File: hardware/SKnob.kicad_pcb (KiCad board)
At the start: 2 copper layers, 61 x 17 mm, 2 parts, among them U1 STM32WLE5JCI6

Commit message: rf network
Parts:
- added C1: C, Capacitor_SMD:C_0402_1005Metric, F.Cu at (126.0, 97.0)
- added C10: C, Capacitor_SMD:C_0402_1005Metric, F.Cu at (116.6, 104.5)
- added C11: C, Capacitor_SMD:C_0402_1005Metric, F.Cu at (123.1, 95.0)
- added C12: C, Capacitor_SMD:C_0402_1005Metric, F.Cu at (128.9, 95.0)
- added C13: C, Capacitor_SMD:C_0402_1005Metric, F.Cu at (119.5, 103.0)
- added C2: C, Capacitor_SMD:C_0402_1005Metric, F.Cu at (108.0, 97.0)
- added C3: C, Capacitor_SMD:C_0402_1005Metric, F.Cu at (120.2, 97.0)
- added C4: C, Capacitor_SMD:C_0402_1005Metric, F.Cu at (106.5, 94.5)
- added C5: C, Capacitor_SMD:C_0402_1005Metric, F.Cu at (106.0, 96.0)
- added C6: C, Capacitor_SMD:C_0402_1005Metric, F.Cu at (123.1, 97.0)
- added C7: C, Capacitor_SMD:C_0402_1005Metric, F.Cu at (126.0, 95.0)
- added C8: C, Capacitor_SMD:C_0402_1005Metric, F.Cu at (120.2, 101.0)
- added C9: C, Capacitor_SMD:C_0402_1005Metric, F.Cu at (123.1, 99.0)
- added L1: L, Inductor_SMD:L_0402_1005Metric, F.Cu at (108.0, 95.0)
- added L2: L, Inductor_SMD:L_0402_1005Metric, F.Cu at (111.5, 99.0)
- added L3: L, Inductor_SMD:L_0402_1005Metric, F.Cu at (119.5, 105.0)
- added L4: L, Inductor_SMD:L_0402_1005Metric, F.Cu at (128.9, 97.0)
- added L5: L, Inductor_SMD:L_0402_1005Metric, F.Cu at (122.5, 103.0)
- added L6: L, Inductor_SMD:L_0402_1005Metric, F.Cu at (126.0, 101.0)
- added U2: BGS12SN6, Package_BGA:Texas_DSBGA-6_0.9x1.4mm_Layout2x3_P0.5mm, F.Cu at (113.2, 103.8)
- moved U1 11.7 mm to (113.0, 95.0), turned to 270 degrees
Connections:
- U1 pad H7: Net-(U1-PadH7) -> /RFI_N
- U1 pad J6: Net-(U1-PadJ6) -> /RFI_P
- U1 pad J8: Net-(U1-PadJ8) -> /RFO_LP

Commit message: stm32wb chip selection
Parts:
- removed C11, C12, C13: C, Capacitor_SMD:C_0402_1005Metric
- removed L4, L5, L6: L, Inductor_SMD:L_0402_1005Metric
- removed U2: BGS12SN6, Package_BGA:Texas_DSBGA-6_0.9x1.4mm_Layout2x3_P0.5mm
- added ANT1: W3008, SKnob:W3008, F.Cu at (104.8, 78.2)
- added J1: USB_B_Micro, Connector_USB:USB_Micro-B_Molex-105133-0001, F.Cu at (124.9, 84.5)
- C1, C2, C3, C4, C7, C8: value C -> 100nF
- C5, C6: value C -> 100pF
- L1, L2: footprint Inductor_SMD:L_0402_1005Metric -> Inductor_SMD:L_0603_1608Metric
- U1: value STM32WLE5JCI6 -> STM32WB55Cx; footprint SKnob:STM32WLE5JCI6 -> SKnob:STM32WB55Cx
- moved L3 24.6 mm to (108.4, 83.0), turned to 180 degrees
- moved C10 24.1 mm to (107.0, 82.4), turned to 90 degrees
- moved L1 21.5 mm to (116.8, 75.4), turned to 0 degrees
- moved C9 21.3 mm to (109.8, 82.4), turned to 90 degrees
- moved C1 21.2 mm to (119.8, 76.8)
- moved C4 20.3 mm to (116.2, 76.8)
- moved C7 19.0 mm to (110.0, 84.8), turned to 270 degrees
- moved C3 17.5 mm to (121.2, 79.5), turned to 270 degrees
- moved C2 16.0 mm to (111.0, 81.2), turned to 90 degrees
- moved C8 14.3 mm to (118.5, 86.8), turned to 180 degrees
- moved L2 14.0 mm to (108.6, 85.3), turned to 270 degrees
- moved U1 13.6 mm to (116.2, 81.8)
- moved C6 13.6 mm to (121.2, 83.5), turned to 270 degrees
- moved C5 12.3 mm to (111.0, 84.8)
- turned BT1 to 0 degrees
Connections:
- C1 pad 1: Net-(C1-Pad1) -> +BATT
- C10 pad 1: Net-(C10-Pad1) -> Net-(ANT1-PadFEED)
- C2 pad 1: /RFI_N -> +BATT
- C2 pad 2: GND -> Net-(C2-Pad2)
- C3 pad 1: Net-(C1-Pad1) -> +BATT
- C3 pad 2: GND -> Net-(C3-Pad2)
- C4 pad 2: /RFI_P -> GND
- C5 pad 1: Net-(C4-Pad1) -> Net-(C5-Pad1)
- C6 pad 1: Net-(C6-Pad1) -> +5V
- C7 pad 1: Net-(C7-Pad1) -> Net-(C5-Pad1)
- C7 pad 2: Net-(C6-Pad1) -> GND
- C8 pad 1: Net-(C7-Pad1) -> +BATT
- C8 pad 2: GND -> Net-(C8-Pad2)
- C9 pad 2: Net-(C7-Pad1) -> GND
- L1 pad 1: /RFI_P -> Net-(C4-Pad1)
- L1 pad 2: /RFI_N -> +BATT
- L2 pad 1: /RFO_LP -> Net-(C5-Pad1)
- L2 pad 2: Net-(C6-Pad1) -> +BATT
- L3 pad 1: Net-(C1-Pad1) -> Net-(C9-Pad1)
- L3 pad 2: Net-(C6-Pad1) -> Net-(ANT1-PadFEED)
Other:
- net class Default: via_dia 0.3 -> 0.5; via_drill 0.1 -> 0.3
- rule pad_to_mask_clearance: 0.05 -> 0

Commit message: preliminary routing
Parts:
- added C11: 100nF, Capacitor_SMD:C_0402_1005Metric, F.Cu at (120.0, 81.7)
- added C12: 100nF, Capacitor_SMD:C_0402_1005Metric, F.Cu at (120.3, 77.1)
- added C13: 4.7uF, Capacitor_SMD:C_0805_2012Metric, F.Cu at (113.6, 87.1)
- added C14: 100nF, Capacitor_SMD:C_0402_1005Metric, F.Cu at (118.0, 86.2)
- added C15: 4.7uF, Capacitor_SMD:C_0805_2012Metric, F.Cu at (119.5, 87.0)
- added C16: C, Capacitor_SMD:C_0402_1005Metric, F.Cu at (111.7, 85.9)
- added C17: C, Capacitor_SMD:C_0402_1005Metric, F.Cu at (117.7, 75.7)
- added C18: C, Capacitor_SMD:C_0402_1005Metric, F.Cu at (109.8, 85.9)
- added C19: C, Capacitor_SMD:C_0402_1005Metric, F.Cu at (115.8, 75.7)
- added C20: 4.7uF, Capacitor_SMD:C_0805_2012Metric, F.Cu at (123.6, 78.3)
- added C21: 100nF, Capacitor_SMD:C_0402_1005Metric, F.Cu at (122.0, 78.2)
- added C22: 100nF, Capacitor_SMD:C_0402_1005Metric, F.Cu at (130.8, 75.6)
- added C23: 4.7uF, Capacitor_SMD:C_0805_2012Metric, F.Cu at (132.4, 75.9)
- added C24: 100nF, Capacitor_SMD:C_0402_1005Metric, F.Cu at (129.8, 75.6)
- added C25: 4.7uF, Capacitor_SMD:C_0805_2012Metric, F.Cu at (130.6, 84.9)
- added C26: 4.7uF, Capacitor_SMD:C_0805_2012Metric, F.Cu at (132.6, 84.9)
- added D1: D, Diode_SMD:D_0603_1608Metric, F.Cu at (120.4, 73.9)
- added D2: TPD4S012DRYR, SKnob:TPD4S012DRYR, F.Cu at (121.2, 83.6)
- added J2: Conn_01x02, Connector_PinHeader_1.00mm:PinHeader_1x02_P1.00mm_Vertical, F.Cu at (125.8, 77.6)
- added J3: Conn_01x02, Connector_PinHeader_1.00mm:PinHeader_1x02_P1.00mm_Vertical, F.Cu at (130.2, 77.6)
- added L4: 600R @ 100MHz, Inductor_SMD:L_0402_1005Metric, F.Cu at (115.6, 85.7)
- added R1: R, Resistor_SMD:R_0402_1005Metric, F.Cu at (121.6, 81.5)
- added R2: R, Resistor_SMD:R_0402_1005Metric, F.Cu at (113.8, 73.0)
- added R3: 10K, Resistor_SMD:R_0402_1005Metric, F.Cu at (111.4, 73.0)
- added R4: 10k, Resistor_SMD:R_0402_1005Metric, F.Cu at (109.1, 73.0)
- added SW1: SW_Push, Button_Switch_SMD:SW_SPST_B3U-3000P, F.Cu at (123.8, 73.9)
- added Y1: 32MHz, Crystal:Crystal_SMD_2016-4Pin_2.0x1.6mm, F.Cu at (110.6, 87.7)
- added Y2: 32MHz, Crystal:Crystal_SMD_2016-4Pin_2.0x1.6mm, F.Cu at (116.8, 73.7)
- BT1: value Battery_Cell -> BR1225
- C1: value 100nF -> C
- C10: value C -> 0.3pF
- C6: value 100pF -> 4.7uF; footprint Capacitor_SMD:C_0402_1005Metric -> Capacitor_SMD:C_0805_2012Metric
- C9: value C -> 0.8pF
- L1, L2: value L -> 600R @ 100MHz
- L3: value L -> 2.7nF
- moved BT1 12.0 mm to (141.0, 80.5)
- moved L1 4.14 mm to (112.8, 74.5), turned to 180 degrees
- moved C1 4.13 mm to (121.6, 80.5), turned to 180 degrees
- moved C10 3.52 mm to (106.1, 79.0), turned to 45 degrees
- moved C6 3.52 mm to (121.6, 87.0)
- moved L3 3.13 mm to (106.7, 80.3), turned to 135 degrees
- moved C4 3.08 mm to (113.4, 75.7), turned to 180 degrees
- moved ANT1 3.05 mm to (104.6, 75.2)
- moved C9 2.23 mm to (108.1, 81.0), turned to 45 degrees
- moved U1 1.84 mm to (114.8, 80.7)
- moved C2 1.82 mm to (109.8, 79.9)
- moved C3 1.75 mm to (120.3, 78.1), turned to 0 degrees
- moved C8 1.63 mm to (117.0, 86.2), turned to 270 degrees
- moved C5 1.32 mm to (109.8, 84.3)
- moved C7 1.32 mm to (108.8, 84.3)
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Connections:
- net Net-(ANT1-PadFEED) renamed /RF1_ANT
- net Net-(C9-Pad1) renamed /RF1
- C1 pad 1: +BATT -> Net-(C1-Pad1)
- C2 pad 2: Net-(C2-Pad2) -> GND
- C3 pad 2: Net-(C3-Pad2) -> GND
- C8 pad 2: Net-(C8-Pad2) -> GND
- J1 pad 1: Net-(J1-Pad1) -> +5V
- J1 pad 2: Net-(J1-Pad2) -> /USB_N
- J1 pad 3: Net-(J1-Pad3) -> /USB_P
- J1 pad 4: Net-(J1-Pad4) -> /ID
- J1 pad 5: Net-(J1-Pad5) -> GND
- J1 pad 6: Net-(J1-Pad6) -> Net-(C1-Pad1)
- U1 pad 2: Net-(U1-Pad2) -> /OSC32_IN
- U1 pad 22: Net-(U1-Pad22) -> GND
- U1 pad 24: Net-(U1-Pad24) -> /OSC_OUT
- U1 pad 25: Net-(U1-Pad25) -> /OSC_IN
- U1 pad 3: Net-(U1-Pad3) -> /OSC32_OUT
- U1 pad 32: Net-(U1-Pad32) -> GND
- U1 pad 34: Net-(U1-Pad34) -> +BATT
- U1 pad 37: Net-(U1-Pad37) -> /USB_N
- U1 pad 38: Net-(U1-Pad38) -> /USB_P
- U1 pad 4: Net-(U1-Pad4) -> /BOOT
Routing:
- net GND: track 0.00 -> 28.4 mm, vias 0 -> 37
- net +BATT: track 0.00 -> 21.1 mm, vias 0 -> 31
- net Net-(D1-Pad2): track 0.00 -> 10.6 mm, vias 0 -> 2
- net /BOOT: track 0.00 -> 9.06 mm, vias 0 -> 2
- net +5V: track 0.00 -> 7.72 mm, vias 0 -> 2
- net /OSC_OUT: track 0.00 -> 5.78 mm
- net Net-(C13-Pad1): track 0.00 -> 4.89 mm
- net /OSC32_IN: track 0.00 -> 4.84 mm
- net /RF1: track 0.00 -> 4.82 mm
- net Net-(C5-Pad1): track 0.00 -> 4.22 mm
- net /RF1_ANT: track 0.00 -> 3.75 mm
- net /OSC_IN: track 0.00 -> 3.47 mm
- net /OSC32_OUT: track 0.00 -> 3.26 mm
- net Net-(C4-Pad1): track 0.00 -> 3.02 mm
- net Net-(D1-Pad1): track 0.00 -> 2.03 mm
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- added copper zone on F.Cu, net +BATT
- added copper zone on In2.Cu, net +BATT
- added copper zone on B.Cu, net GND
- added copper zone on F.Cu, net GND
- added copper zone on In1.Cu, net GND
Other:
- board size 61 x 17 mm -> 50 x 17 mm
- copper layers 2 -> 4
- net class Default: via_dia 0.5 -> 0.45; via_drill 0.3 -> 0.2
- net class microstrip added: clearance 0.3, trace_width 0.29337, via_dia 0.45, via_drill 0.2
- net class pwr added: clearance 0.15, trace_width 0.3, via_dia 0.6, via_drill 0.3
- rule trace_min: 0.15 -> 0.127

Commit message: added accel
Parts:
- added C27: 100nF, Capacitor_SMD:C_0402_1005Metric, F.Cu at (109.4, 77.4)
- added U2: LIS2DE12TR, SKnob:LIS2DE12TR, F.Cu at (109.4, 75.6)
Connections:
- U1 pad 5: Net-(U1-Pad5) -> /I2C1_SCL
- U1 pad 6: Net-(U1-Pad6) -> /I2C1_SDA
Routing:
- net /I2C1_SDA: track 0.00 -> 9.03 mm, vias 0 -> 2
- net /I2C1_SCL: track 0.00 -> 8.65 mm, vias 0 -> 2
- net GND: track 28.4 -> 32.0 mm, vias 37 -> 38
- net +BATT: track 21.1 -> 24.1 mm, vias 31 -> 32

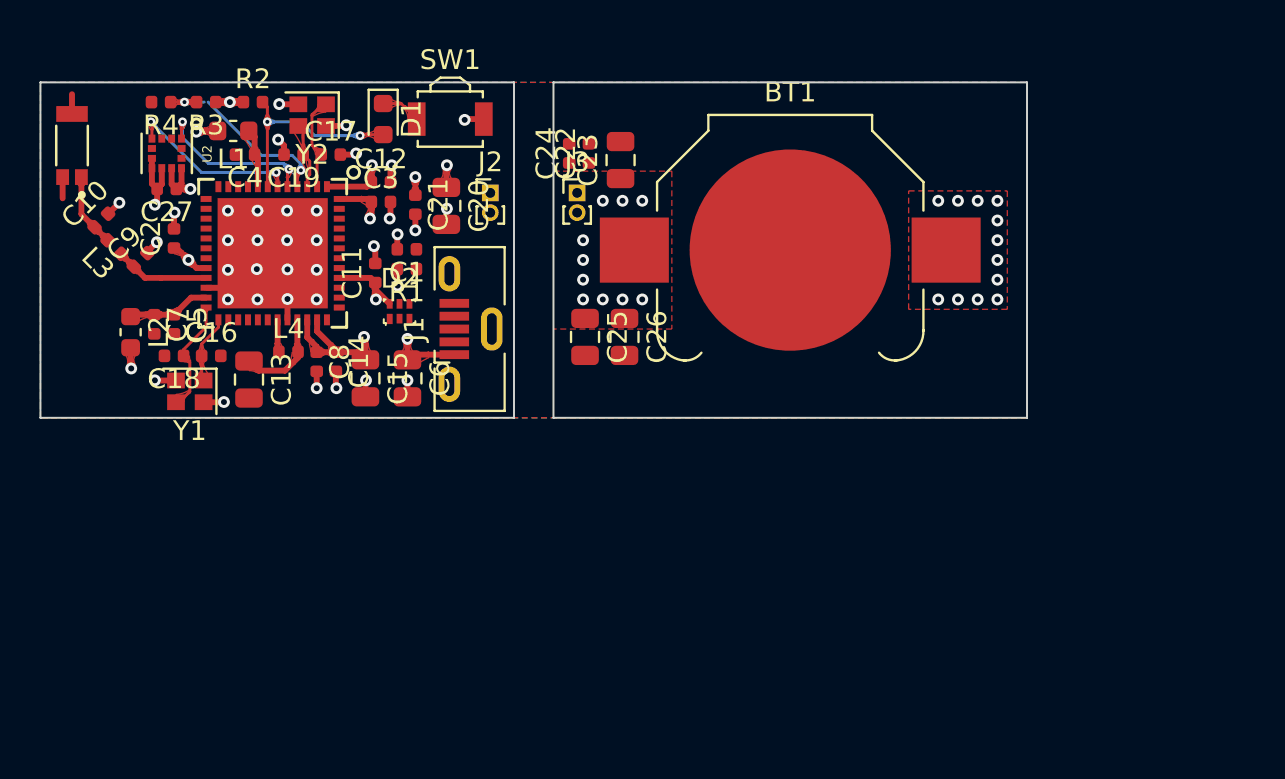
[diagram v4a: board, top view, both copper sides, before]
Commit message: update hardware to include test points in the back and commit auto generated firmware project files
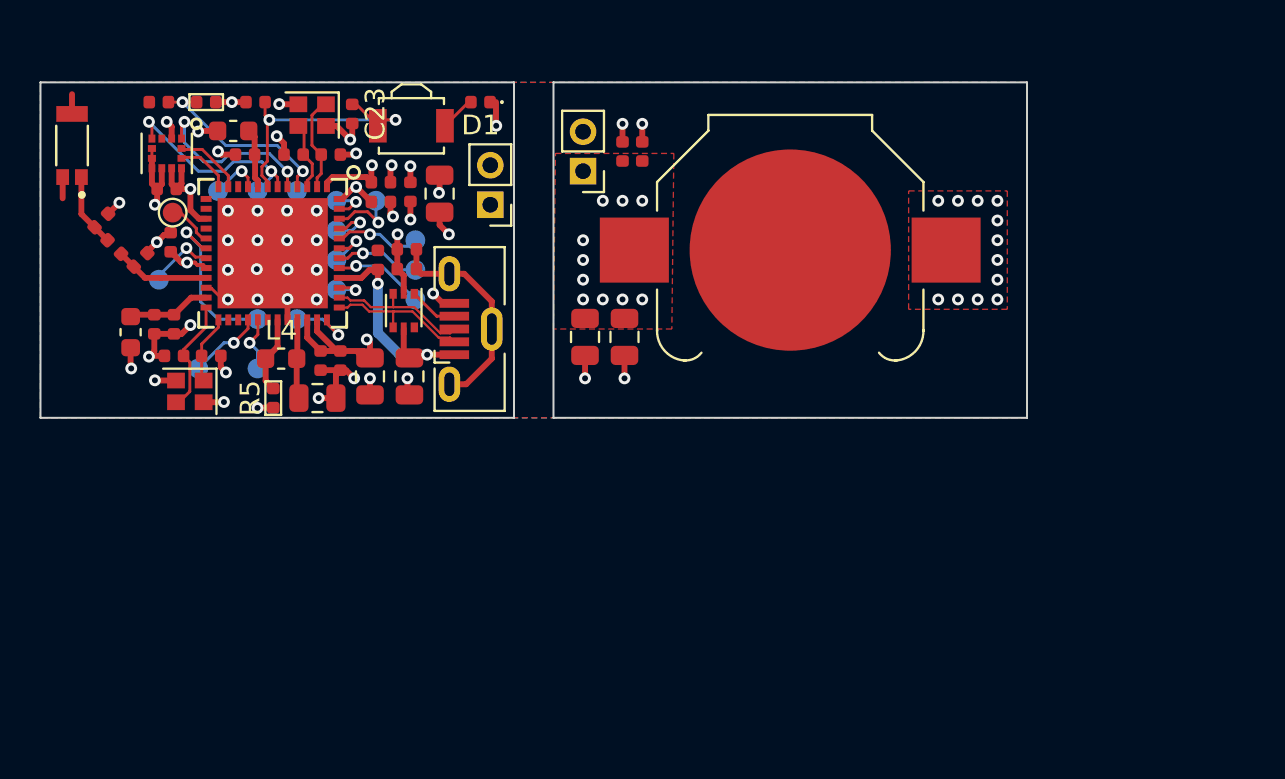
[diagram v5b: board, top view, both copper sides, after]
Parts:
- removed D2: TPD4S012DRYR, SKnob:TPD4S012DRYR
- added R5: 0, SKnob:R_0402_1005Metric_DNP, F.Cu at (114.8, 88.0)
- added T1: LA_LOGO, SKnob:LA_LOGO, F.Cu at (105.5, 87.0)
- added T2: LA_LOGO, SKnob:LA_LOGO, F.Cu at (150.5, 87.0)
- added TP1: TestPoint, SKnob:TestPoint_Pad_D1.0mm, F.Cu at (109.7, 78.6)
- added TP10: TestPoint, SKnob:TestPoint_Pad_D1.0mm, B.Cu at (122.0, 80.0)
- added TP11: TestPoint, SKnob:TestPoint_Pad_D1.0mm, B.Cu at (118.0, 79.5)
- added TP12: TestPoint, SKnob:TestPoint_Pad_D1.0mm, B.Cu at (120.0, 78.0)
- added TP13: TestPoint, SKnob:TestPoint_Pad_D1.0mm, B.Cu at (118.0, 78.0)
- added TP14: TestPoint, SKnob:TestPoint_Pad_D1.0mm, B.Cu at (118.0, 82.5)
- added TP15: TestPoint, SKnob:TestPoint_Pad_D1.0mm, B.Cu at (122.0, 83.0)
- added TP16: TestPoint, SKnob:TestPoint_Pad_D1.0mm, B.Cu at (122.0, 81.5)
- added TP17: TestPoint, SKnob:TestPoint_Pad_D1.0mm, B.Cu at (112.0, 77.5)
- added TP2: TestPoint, SKnob:TestPoint_Pad_D1.0mm, B.Cu at (116.0, 77.5)
- added TP3: TestPoint, SKnob:TestPoint_Pad_D1.0mm, B.Cu at (114.0, 77.5)
- added TP4: TestPoint, SKnob:TestPoint_Pad_D1.0mm, B.Cu at (114.0, 84.0)
- added TP5: TestPoint, SKnob:TestPoint_Pad_D1.0mm, B.Cu at (116.0, 84.0)
- added TP6: TestPoint, SKnob:TestPoint_Pad_D1.0mm, B.Cu at (111.0, 86.5)
- added TP7: TestPoint, SKnob:TestPoint_Pad_D1.0mm, B.Cu at (114.0, 86.5)
- added TP8: TestPoint, SKnob:TestPoint_Pad_D1.0mm, B.Cu at (109.0, 82.0)
- added TP9: TestPoint, SKnob:TestPoint_Pad_D1.0mm, B.Cu at (118.0, 81.0)
- added U3: USBLC6-2P6, Package_TO_SOT_SMD:SOT-666, F.Cu at (121.4, 83.6)
- C16, C17, C18, C19: value C -> 4.3pF
- C23: value 4.7uF -> 100nF; footprint Capacitor_SMD:C_0805_2012Metric -> Capacitor_SMD:C_0402_1005Metric
- D1: value D -> 1N4148; footprint Diode_SMD:D_0603_1608Metric -> Diode_SMD:D_0402_1005Metric
- J2, J3: footprint Connector_PinHeader_1.00mm:PinHeader_1x02_P1.00mm_Vertical -> Connector_PinHeader_2.00mm:PinHeader_1x02_P2.00mm_Vertical
- L4: value 600R @ 100MHz -> 10uH; footprint Inductor_SMD:L_0402_1005Metric -> Inductor_SMD:L_0603_1608Metric
- R2: value R -> 10k
- R3: footprint Resistor_SMD:R_0402_1005Metric -> SKnob:R_0402_1005Metric_DNP
- Y2: value 32MHz -> 32.768kHz
- moved C23 13.8 mm to (118.8, 73.6), turned to 270 degrees
- moved D1 5.00 mm to (125.3, 73.0), turned to 180 degrees
- moved C13 3.59 mm to (117.0, 88.0), turned to 0 degrees
- moved C22 2.70 mm to (133.5, 75.5)
- moved C24 2.70 mm to (132.5, 75.5)
- moved SW1 2.00 mm to (121.8, 74.2)
- moved J3 1.14 mm to (130.5, 76.5), turned to 180 degrees
- moved C20 0.71 mm to (123.2, 77.6), turned to 90 degrees
- moved C21 0.70 mm to (121.8, 77.5), turned to 90 degrees
- moved C11 0.67 mm to (120.1, 81.0)
- moved J2 0.60 mm to (125.8, 78.2), turned to 180 degrees
- moved L4 0.50 mm to (115.2, 86.0)
- moved C2 0.25 mm to (109.6, 80.1)
- moved C15 0.25 mm to (119.7, 86.9)
- moved C14 0.24 mm to (118.2, 86.1)
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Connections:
- net Net-(C4-Pad1) renamed /VDDA
- net Net-(C5-Pad1) renamed /VDDRF
- C23 pad 1: +BATT -> /RST_N
- D1 pad 1: Net-(D1-Pad1) -> GND
- R2 pad 2: Net-(D1-Pad2) -> /RST_N
- SW1 pad 1: Net-(D1-Pad1) -> /RST_N
- SW1 pad 2: GND -> Net-(D1-Pad2)
- U1 pad 11: Net-(U1-Pad11) -> /ACC_INT1
- U1 pad 12: Net-(U1-Pad12) -> /ACC_INT2
- U1 pad 15: Net-(U1-Pad15) -> +BATT
- U1 pad 17: Net-(U1-Pad17) -> /RCC_MCO
- U1 pad 18: Net-(U1-Pad18) -> /USART1_TX
- U1 pad 19: Net-(U1-Pad19) -> /PB2
- U1 pad 28: Net-(U1-Pad28) -> /PB0
- U1 pad 29: Net-(U1-Pad29) -> /PB1
- U1 pad 36: Net-(U1-Pad36) -> /USART1_RX
- U1 pad 39: Net-(U1-Pad39) -> /JTMS-SWDIO
- U1 pad 41: Net-(U1-Pad41) -> /JTCK-SWCLK
- U1 pad 42: Net-(U1-Pad42) -> /JTDI
- U1 pad 43: Net-(U1-Pad43) -> /PB3_JTDO-SWO
- U1 pad 44: Net-(U1-Pad44) -> /PB4_JTRST
- U1 pad 45: Net-(U1-Pad45) -> /PB5
- U1 pad 46: Net-(U1-Pad46) -> /PB6
- U1 pad 47: Net-(U1-Pad47) -> /PB7
- U1 pad 7: Net-(D1-Pad2) -> /RST_N
- U1 pad 9: Net-(U1-Pad9) -> /WKUP1
- U2 pad 11: Net-(U2-Pad11) -> /ACC_INT2
- U2 pad 12: Net-(U2-Pad12) -> /ACC_INT1
- U2 pad 2: Net-(U2-Pad2) -> +BATT
- U2 pad 5: Net-(U2-Pad5) -> GND
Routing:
- net GND: track 32.0 -> 48.8 mm, vias 38 -> 45
- net /RST_N: track 0.00 -> 13.8 mm, vias 0 -> 2
- net Net-(C1-Pad1): track 0.00 -> 11.1 mm
- net Net-(D1-Pad2): track 10.6 -> 1.81 mm, vias 2 -> 0
- net /USART1_TX: track 0.00 -> 8.39 mm, vias 0 -> 1
- net /USB_N: track 0.00 -> 7.48 mm
- net /USB_P: track 0.00 -> 7.35 mm
- net +5V: track 7.72 -> 12.4 mm
- net +BATT: track 24.1 -> 28.8 mm, vias 32 -> 33
- net /JTCK-SWCLK: track 0.00 -> 4.60 mm, vias 0 -> 1
- net /PB4_JTRST: track 0.00 -> 4.42 mm, vias 0 -> 1
- net /JTDI: track 0.00 -> 4.30 mm, vias 0 -> 1
- net /PB0: track 0.00 -> 3.80 mm, vias 0 -> 1
- net /PB6: track 0.00 -> 3.50 mm, vias 0 -> 1
- net /ACC_INT1: track 0.00 -> 3.50 mm
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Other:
- net class Default: clearance 0.15 -> 0.1; via_dia 0.45 -> 0.6; via_drill 0.2 -> 0.3
- net class microstrip: via_dia 0.45 -> 0.6; via_drill 0.2 -> 0.3
- net class pwr: clearance 0.15 -> 0.1
- net class usb added: clearance 0.1, trace_width 0.118, via_dia 0.6, via_drill 0.3
- rule trace_clearance: 0.15 -> 0.1
- rule trace_min: 0.127 -> 0.1
- board text added: "0"
- board text added: "1"
- board text added: "2"
- board text added: "3-JTDO-SWO"
- board text added: "4-JTRST"
- board text added: "5"
- board text added: "6"
- board text added: "7"
- board text added: "JTCK-SWCLK"
- board text added: "JTDI"
- board text added: "JTMS-SWDIO"
- board text added: "RX"
- board text added: "SCL"
- board text added: "SDA"
- board text added: "SKnob"
- board text added: "TX"
- board text added: "WKUP"

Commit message: finishing touches
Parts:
- removed C10: 0.3pF, Capacitor_SMD:C_0402_1005Metric
- removed C9: 0.8pF, Capacitor_SMD:C_0402_1005Metric
- removed L3: 2.7nF, Inductor_SMD:L_0402_1005Metric
- added BATT?1: BR1225, SKnob:BR1225, F.Cu at (140.9, 80.3)
- added FLT1: MLPF-WB55-01E3, SKnob:MLPF-WB55-01E3, F.Cu at (109.5, 82.4)
- added QR*****: bozica.co, SKnob:bozica.co, B.Cu at (141.4, 80.4)
- added TP18: TestPoint, SKnob:TestPoint_Pad_D1.0mm, B.Cu at (111.8, 77.5)
- added TP19: TestPoint, SKnob:TestPoint_Pad_D1.0mm, B.Cu at (109.5, 77.5)
- BT1: value BR1225 -> BK-885-TR
- C16, C17, C18, C19: value 4.3pF -> 15pF
- moved T2 10.6 mm to (150.3, 76.4)
- moved TP17 1.25 mm to (113.2, 77.5)
- moved T1 1.06 mm to (104.8, 86.2), turned to 270 degrees
- moved TP3 0.75 mm to (114.8, 77.5)
- moved TP2 0.25 mm to (116.2, 77.5)
- moved L2 0.18 mm to (107.6, 84.8)
- moved J2 0.10 mm to (125.7, 78.2)
- moved TP1 0.07 mm to (109.7, 78.5)
- moved C5 0.07 mm to (109.8, 84.3)
- moved C7 0.07 mm to (108.8, 84.3)
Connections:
- U1 pad 11: /ACC_INT1 -> /LPUART1_TX
- U1 pad 12: /ACC_INT2 -> /LPUART1_RX
- U1 pad 13: Net-(U1-Pad13) -> /ACC_INT1
- U1 pad 14: Net-(U1-Pad14) -> /ACC_INT2
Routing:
- net /RF1_ANT: track 3.75 -> 7.61 mm
- net /RF1: track 4.82 -> 1.28 mm
- net /LPUART1_RX: track 0.00 -> 3.41 mm, vias 0 -> 1
- net /LPUART1_TX: track 0.00 -> 2.10 mm, vias 0 -> 1
- net GND: track 48.8 -> 47.3 mm, vias 45 -> 71
- net /WKUP1: track 2.73 -> 1.94 mm
- net +BATT: track 28.8 -> 29.5 mm, vias 33 -> 35
- net /I2C1_SDA: track 10.7 -> 10.1 mm
- net /ACC_INT2: track 2.84 -> 3.39 mm
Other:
- board text added: "+BATT"
- board text added: "GND"
- board text added: "Rev 1.0 2020-08-02"
- board text added: "USART"
- board text added: "bozica.co"
